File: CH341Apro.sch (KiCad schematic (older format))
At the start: 17 parts, among them J1 USB_A, J3 ZIF-16, J4 , J5 V_SEL, U1 AMS1117-3.3, U2 CH341a, Y1 12M

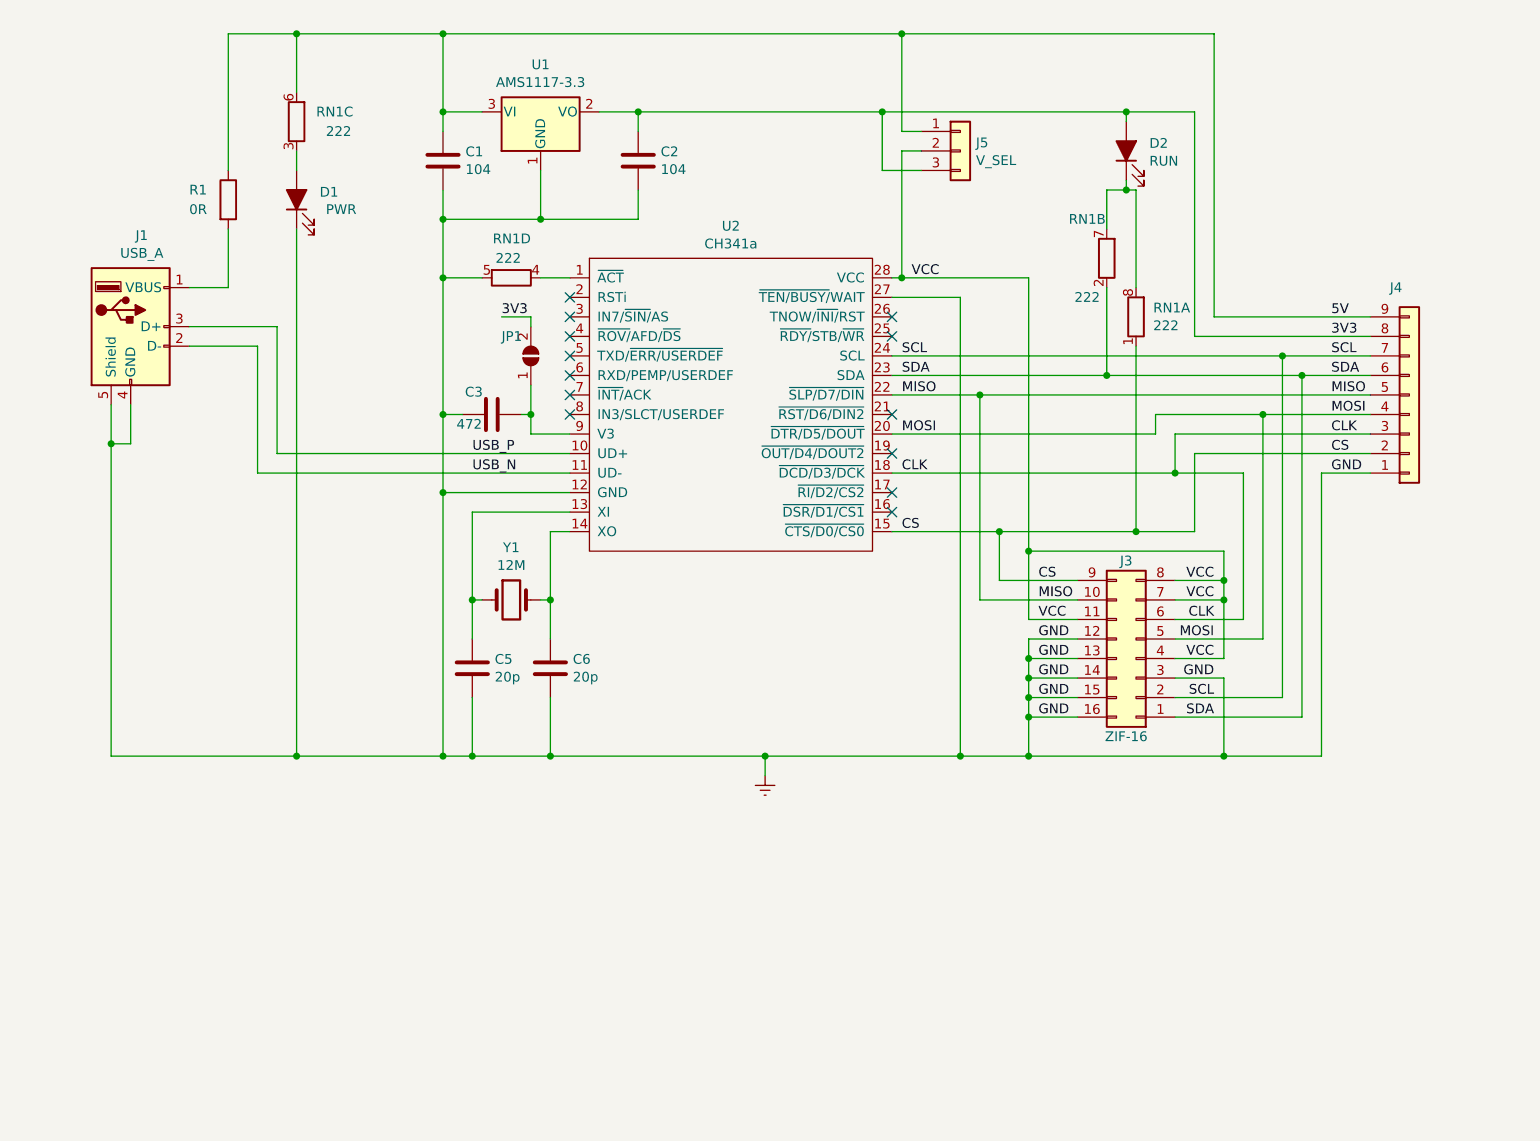
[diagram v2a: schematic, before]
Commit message: Major ergo change
Updated components footprints for hand soldering.
Change VCC routing.
Add JP1/2 for selecting operating voltage.
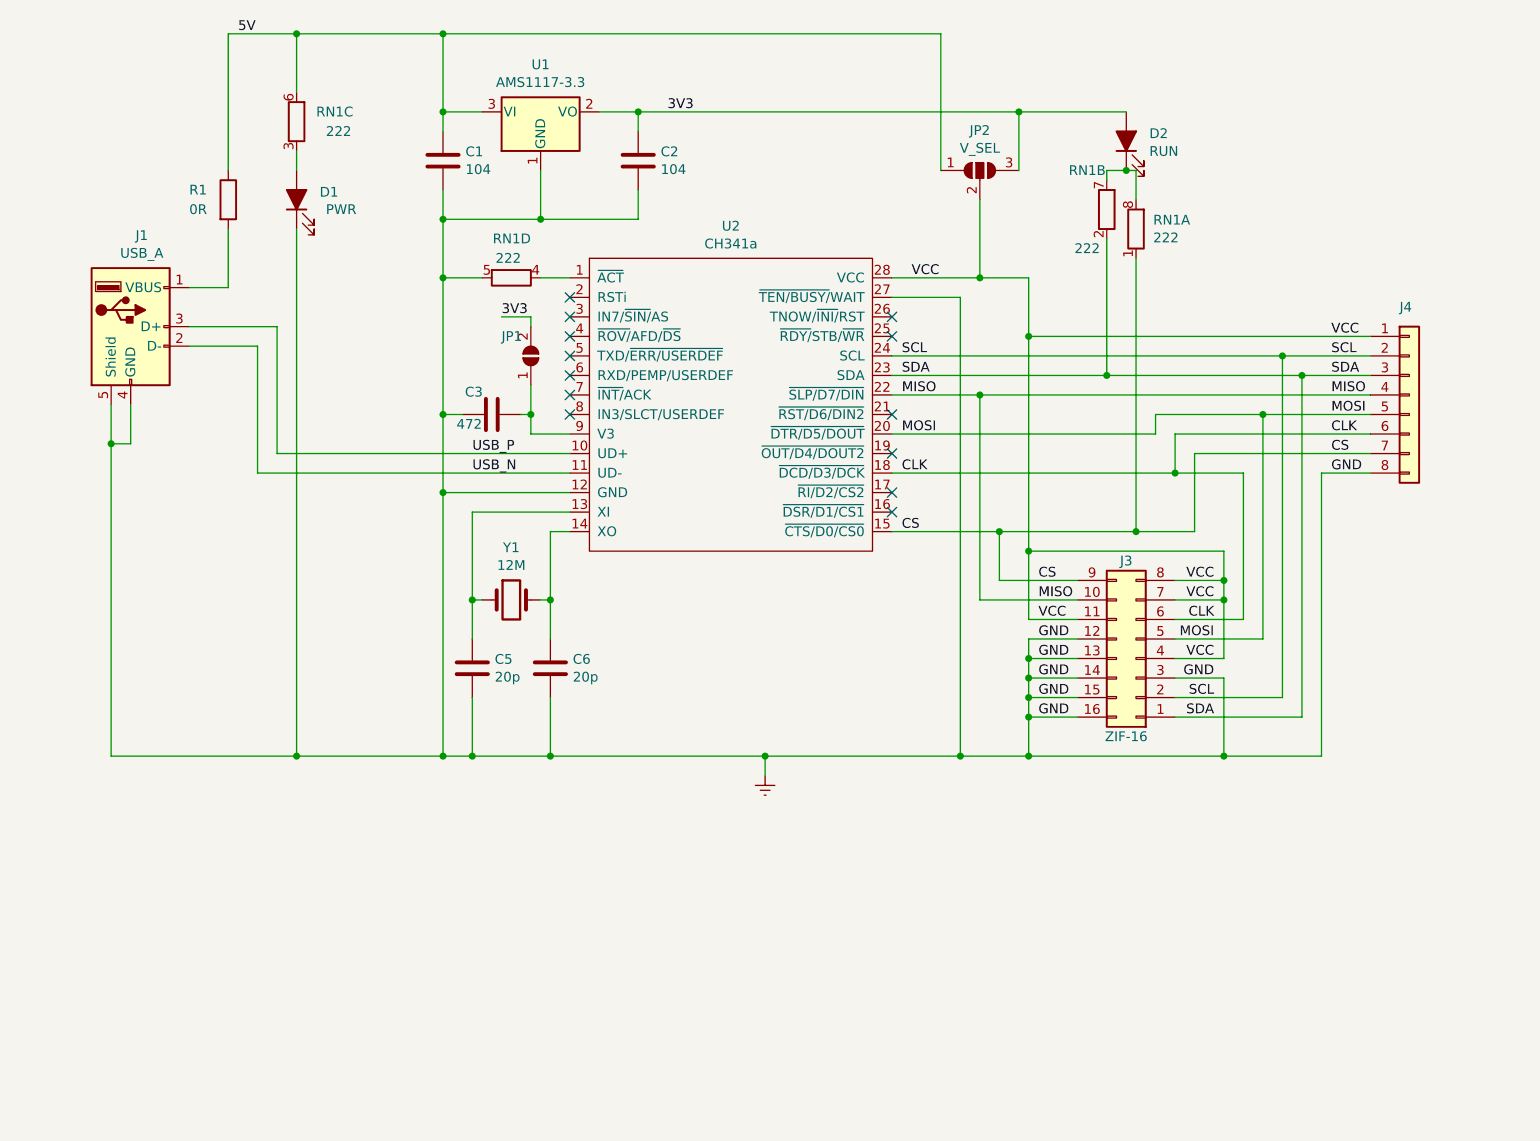
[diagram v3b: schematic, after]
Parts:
- removed J4: (no value), Connector_PinHeader_2.54mm:PinHeader_1x09_P2.54mm_Vertical, symbol Connector_Generic:Conn_01x09
- removed J5: V_SEL, Connector_PinHeader_2.54mm:PinHeader_1x03_P2.54mm_Vertical, symbol Connector_Generic:Conn_01x03
- added J4: (no value), Connector_PinHeader_2.54mm:PinHeader_1x08_P2.54mm_Vertical, symbol Connector_Generic:Conn_01x08
- added JP2: V_SEL, Jumper:SolderJumper-3_P1.3mm_Open_RoundedPad1.0x1.5mm_NumberLabels, symbol Jumper:SolderJumper_3_Open
- C1, C2, C3: footprint Capacitor_SMD:C_0603_1608Metric -> Capacitor_SMD:C_0603_1608Metric_Pad1.05x0.95mm_HandSolder
- C5, C6: footprint Capacitor_SMD:C_0402_1005Metric -> Capacitor_SMD:C_0603_1608Metric_Pad1.05x0.95mm_HandSolder
- D1, D2: footprint LED_SMD:LED_0603_1608Metric -> LED_SMD:LED_0603_1608Metric_Castellated
- JP1: footprint Jumper:SolderJumper-2_P1.3mm_Open_Pad1.0x1.5mm -> Jumper:SolderJumper-2_P1.3mm_Open_RoundedPad1.0x1.5mm
- R1: footprint Resistor_SMD:R_0603_1608Metric -> Resistor_SMD:R_0603_1608Metric_Pad0.98x0.95mm_HandSolder
- Y1: footprint Crystal:Crystal_SMD_5032-2Pin_5.0x3.2mm -> Crystal:Crystal_SMD_5032-2Pin_5.0x3.2mm_HandSoldering
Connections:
- net 3V3: now also JP2.3 (B)
- net 5V: now also JP2.1 (A)
- net CLK: now also J4.6 (Pin_6)
- net CS: now also J4.7 (Pin_7)
- net Earth: now also J4.8 (Pin_8)
- net MISO: now also J4.4 (Pin_4)
- net MOSI: now also J4.5 (Pin_5)
- net SCL: now also J4.2 (Pin_2)
- net SDA: now also J4.3 (Pin_3)
- net VCC: now also J4.1 (Pin_1), JP2.2 (C)
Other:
- moved on the sheet: D2, RN1A, RN1B
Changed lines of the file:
@@
 Sheet 1 1
 Title "CH341A Programmer"
-Date "2021-02-26"
-Rev "V0.2"
+Date "2021-03-12"
+Rev "V0.2a"
 Comp "JackCarterSmith originally from Ray Tracer / Jake L"
 Comment1 ""
@@
 F 0 "R1" H 1150 1550 50  0000 L CNN
 F 1 "0R" H 1150 1450 50  0000 L CNN
-F 2 "Resistor_SMD:R_0603_1608Metric" V 1280 1500 50  0001 C CNN
+F 2 "Resistor_SMD:R_0603_1608Metric_Pad0.98x0.95mm_HandSolder" V 1280 1500 50  0001 C CNN
 F 3 "~" H 1350 1500 50  0001 C CNN
 F 4 "C207010" H 1350 1500 50  0001 C CNN "LCSC"
@@
 L Device:R_Pack04_Split RN1
 U 1 1 5F0C60C3
-P 6000 2100
-F 0 "RN1" H 6088 2146 50  0000 L CNN
-F 1 "222" H 6088 2055 50  0000 L CNN
-F 2 "Resistor_SMD:R_Array_Convex_4x0603" V 5920 2100 50  0001 C CNN
-F 3 "~" H 6000 2100 50  0001 C CNN
-F 4 "C12001" H 6000 2100 50  0001 C CNN "LCSC"
-	1    6000 2100
+P 6000 1650
+F 0 "RN1" H 6088 1696 50  0000 L CNN
+F 1 "222" H 6088 1605 50  0000 L CNN
+F 2 "Resistor_SMD:R_Array_Convex_4x0603" V 5920 1650 50  0001 C CNN
+F 3 "~" H 6000 1650 50  0001 C CNN
+F 4 "C12001" H 6000 1650 50  0001 C CNN "LCSC"
+	1    6000 1650
 	1    0    0    -1
 $EndComp
@@
 L Device:R_Pack04_Split RN1
 U 2 1 5F0C7BA5
-P 5850 1800
-F 0 "RN1" H 5750 2000 50  0000 C CNN
-F 1 "222" H 5750 1600 50  0000 C CNN
-F 2 "Resistor_SMD:R_Array_Convex_4x0603" V 5770 1800 50  0001 C CNN
-F 3 "~" H 5850 1800 50  0001 C CNN
-F 4 "C12001" H 5850 1800 50  0001 C CNN "LCSC"
-	2    5850 1800
+P 5850 1550
+F 0 "RN1" H 5750 1750 50  0000 C CNN
+F 1 "222" H 5750 1350 50  0000 C CNN
+F 2 "Resistor_SMD:R_Array_Convex_4x0603" V 5770 1550 50  0001 C CNN
+F 3 "~" H 5850 1550 50  0001 C CNN
+F 4 "C12001" H 5850 1550 50  0001 C CNN "LCSC"
+	2    5850 1550
 	1    0    0    -1
 $EndComp
@@
 F 0 "C1" H 2565 1346 50  0000 L CNN
 F 1 "104" H 2565 1255 50  0000 L CNN
-F 2 "Capacitor_SMD:C_0603_1608Metric" H 2488 1150 50  0001 C CNN
+F 2 "Capacitor_SMD:C_0603_1608Metric_Pad1.05x0.95mm_HandSolder" H 2488 1150 50  0001 C CNN
 F 3 "~" H 2450 1300 50  0001 C CNN
 F 4 "C19702" H 2450 1300 50  0001 C CNN "LCSC"
@@
 L Device:LED_ALT D2
 U 1 1 5F0CEBAD
-P 5950 1250
-F 0 "D2" V 5989 1132 50  0000 R CNN
-F 1 "RUN" V 5898 1132 50  0000 R CNN
-F 2 "LED_SMD:LED_0603_1608Metric" H 5950 1250 50  0001 C CNN
-F 3 "~" H 5950 1250 50  0001 C CNN
-F 4 "C72043" V 5950 1250 50  0001 C CNN "LCSC"
-	1    5950 1250
+P 5950 1200
+F 0 "D2" V 5989 1082 50  0000 R CNN
+F 1 "RUN" V 5898 1082 50  0000 R CNN
+F 2 "LED_SMD:LED_0603_1608Metric_Castellated" H 5950 1200 50  0001 C CNN
+F 3 "~" H 5950 1200 50  0001 C CNN
+F 4 "C72043" V 5950 1200 50  0001 C CNN "LCSC"
+	1    5950 1200
 	0    -1   -1   0
 $EndComp
-Wire Wire Line
-	5850 1650 5850 1450
-Wire Wire Line
-	5850 1450 5950 1450
-Wire Wire Line
-	5950 1450 5950 1400
-Wire Wire Line
-	5950 1450 6000 1450
-Wire Wire Line
-	6000 1450 6000 1950
-Connection ~ 5950 1450
 $Comp
 L Device:LED_ALT D1
@@
 F 0 "D1" V 1739 1382 50  0000 R CNN
 F 1 "PWR" V 1650 1350 50  0000 R CNN
-F 2 "LED_SMD:LED_0603_1608Metric" H 1700 1500 50  0001 C CNN
+F 2 "LED_SMD:LED_0603_1608Metric_Castellated" H 1700 1500 50  0001 C CNN
 F 3 "~" H 1700 1500 50  0001 C CNN
 F 4 "C72044" V 1700 1500 50  0001 C CNN "LCSC"
@@
 F 0 "C2" H 3565 1346 50  0000 L CNN
 F 1 "104" H 3565 1255 50  0000 L CNN
-F 2 "Capacitor_SMD:C_0603_1608Metric" H 3488 1150 50  0001 C CNN
+F 2 "Capacitor_SMD:C_0603_1608Metric_Pad1.05x0.95mm_HandSolder" H 3488 1150 50  0001 C CNN
 F 3 "~" H 3450 1300 50  0001 C CNN
 F 4 "C19702" H 3450 1300 50  0001 C CNN "LCSC"
@@
 F 0 "Y1" H 2800 3818 50  0000 C CNN
 F 1 "12M" H 2800 3727 50  0000 C CNN
-F 2 "Crystal:Crystal_SMD_5032-2Pin_5.0x3.2mm" H 2800 3550 50  0001 C CNN
+F 2 "Crystal:Crystal_SMD_5032-2Pin_5.0x3.2mm_HandSoldering" H 2800 3550 50  0001 C CNN
 F 3 "~" H 2800 3550 50  0001 C CNN
 F 4 "C112573" H 2800 3550 50  0001 C CNN "LCSC"
@@
 F 0 "C5" H 2715 3946 50  0000 L CNN
 F 1 "20p" H 2715 3855 50  0000 L CNN
-F 2 "Capacitor_SMD:C_0402_1005Metric" H 2638 3750 50  0001 C CNN
+F 2 "Capacitor_SMD:C_0603_1608Metric_Pad1.05x0.95mm_HandSolder" H 2638 3750 50  0001 C CNN
 F 3 "~" H 2600 3900 50  0001 C CNN
 F 4 "C1554" H 2600 3900 50  0001 C CNN "LCSC"
@@
 F 0 "C6" H 3115 3946 50  0000 L CNN
 F 1 "20p" H 3115 3855 50  0000 L CNN
-F 2 "Capacitor_SMD:C_0402_1005Metric" H 3038 3750 50  0001 C CNN
+F 2 "Capacitor_SMD:C_0603_1608Metric_Pad1.05x0.95mm_HandSolder" H 3038 3750 50  0001 C CNN
 F 3 "~" H 3000 3900 50  0001 C CNN
 F 4 "C1554" H 3000 3900 50  0001 C CNN "LCSC"
@@
 	1    0    0    -1
 $EndComp
-Wire Wire Line
-	5850 2400 5850 1950
 $Comp
 L power:Earth #PWR01
@@
 Wire Wire Line
 	2450 1050 2450 650
-Wire Wire Line
-	5950 1100 5950 1050
-Connection ~ 5950 1050
-Wire Wire Line
-	5950 1050 6300 1050
-Text Label 7000 2200 0    50   ~ 0
-3V3
 Text Label 7000 2900 0    50   ~ 0
 GND
@@
 Text Label 7000 2700 0    50   ~ 0
 CLK
-Text Label 7000 2100 0    50   ~ 0
-5V
-Wire Wire Line
-	6400 650  6400 2100
-Wire Wire Line
-	6300 1050 6300 2200
+Text Label 7000 2200 0    50   ~ 0
+VCC
 Text Label 5500 3550 0    50   ~ 0
 MISO
@@
 	750  2550 750  2750
 Connection ~ 750  2750
-Wire Wire Line
-	4750 1900 4800 1900
-Wire Wire Line
-	4800 1900 4800 1250
-Wire Wire Line
-	4800 1250 4900 1250
-Wire Wire Line
-	4900 1350 4700 1350
-Wire Wire Line
-	4700 1350 4700 1050
-Wire Wire Line
-	4900 1150 4800 1150
-Wire Wire Line
-	4800 1150 4800 650
-Connection ~ 4800 650
-Wire Wire Line
-	4800 650  6400 650
 Text Label 2750 2100 0    50   ~ 0
 3V3
@@
 Wire Wire Line
 	2450 1600 2950 1600
-Wire Wire Line
-	2450 650  4800 650
-Wire Wire Line
-	3450 1050 4700 1050
 Connection ~ 3450 1050
-Connection ~ 4700 1050
 Text Label 5500 3850 0    50   ~ 0
 GND
@@
 Wire Wire Line
 	4750 2900 6200 2900
-$Comp
-L Connector_Generic:Conn_01x09 J4
-U 1 1 603FB5BA
-P 7400 2500
-F 0 "J4" H 7300 1950 50  0000 L CNN
-F 1 " " H 7480 2451 50  0000 L CNN
-F 2 "Connector_PinHeader_2.54mm:PinHeader_1x09_P2.54mm_Vertical" H 7400 2500 50  0001 C CNN
-F 3 "~" H 7400 2500 50  0001 C CNN
-	1    7400 2500
-	1    0    0    1
-$EndComp
-Wire Wire Line
-	7200 2100 6400 2100
-$Comp
-L Connector_Generic:Conn_01x03 J5
-U 1 1 604046DB
-P 5100 1250
-F 0 "J5" H 5180 1292 50  0000 L CNN
-F 1 "V_SEL" H 5180 1201 50  0000 L CNN
-F 2 "Connector_PinHeader_2.54mm:PinHeader_1x03_P2.54mm_Vertical" H 5100 1250 50  0001 C CNN
-F 3 "~" H 5100 1250 50  0001 C CNN
-	1    5100 1250
-	1    0    0    -1
-$EndComp
 Wire Wire Line
 	4750 2400 5850 2400
@@
 Wire Wire Line
 	5450 3650 5450 3300
-Wire Wire Line
-	7200 2200 6300 2200
 Wire Wire Line
 	6450 3450 6450 3300
@@
 SDA
 Wire Wire Line
-	6000 2250 6000 3200
-Wire Wire Line
 	7200 2900 6950 2900
 Wire Wire Line
@@
 	6650 2600 6100 2600
 Wire Wire Line
-	4700 1050 5950 1050
-Wire Wire Line
-	4800 1900 5450 1900
-Wire Wire Line
-	5450 1900 5450 3300
-Connection ~ 4800 1900
+	5450 1900 5450 2200
 Connection ~ 5450 3300
 Text Label 4850 1900 0    50   ~ 0
@@
 F 0 "C3" V 2815 2646 50  0000 L CNN
 F 1 "472" V 2650 2650 50  0000 L CNN
-F 2 "Capacitor_SMD:C_0603_1608Metric" H 2738 2450 50  0001 C CNN
+F 2 "Capacitor_SMD:C_0603_1608Metric_Pad1.05x0.95mm_HandSolder" H 2738 2450 50  0001 C CNN
 F 3 "~" H 2700 2600 50  0001 C CNN
 F 4 "C8032" V 2700 2600 50  0001 C CNN "LCSC"
@@
 F 0 "JP1" V 3000 2450 50  0000 R CNN
 F 1 " " V 2855 2212 50  0000 R CNN
-F 2 "Jumper:SolderJumper-2_P1.3mm_Open_Pad1.0x1.5mm" H 2900 2300 50  0001 C CNN
+F 2 "Jumper:SolderJumper-2_P1.3mm_Open_RoundedPad1.0x1.5mm" H 2900 2300 50  0001 C CNN
 F 3 "~" H 2900 2300 50  0001 C CNN
 	1    2900 2300
 	0    -1   -1   0
 $EndComp
+$Comp
+L Jumper:SolderJumper_3_Open JP2
+U 1 1 604BEDAC
+P 5200 1350
+F 0 "JP2" H 5200 1555 50  0000 C CNN
+F 1 "V_SEL" H 5200 1464 50  0000 C CNN
+F 2 "Jumper:SolderJumper-3_P1.3mm_Open_RoundedPad1.0x1.5mm_NumberLabels" H 5200 1350 50  0001 C CNN
+F 3 "~" H 5200 1350 50  0001 C CNN
+	1    5200 1350
+	1    0    0    -1
+$EndComp
+Wire Wire Line
+	2450 650  5000 650
+Wire Wire Line
+	4750 1900 5200 1900
+Wire Wire Line
+	5200 1500 5200 1900
+Connection ~ 5200 1900
+Wire Wire Line
+	5200 1900 5450 1900
+$Comp
+L Connector_Generic:Conn_01x08 J4
+U 1 1 604F57DB
+P 7400 2500
+F 0 "J4" H 7350 2950 50  0000 L CNN
+F 1 " " H 7480 2401 50  0000 L CNN
+F 2 "Connector_PinHeader_2.54mm:PinHeader_1x08_P2.54mm_Vertical" H 7400 2500 50  0001 C CNN
+F 3 "~" H 7400 2500 50  0001 C CNN
+	1    7400 2500
+	1    0    0    -1
+$EndComp
+Wire Wire Line
+	3450 1050 5400 1050
+Wire Wire Line
+	5000 1350 5000 650
+Wire Wire Line
+	5400 1350 5400 1050
+Connection ~ 5400 1050
+Wire Wire Line
+	5400 1050 5950 1050
+Wire Wire Line
+	5950 1350 5850 1350
+Wire Wire Line
+	5850 1350 5850 1400
+Wire Wire Line
+	5950 1350 6000 1350
+Wire Wire Line
+	6000 1350 6000 1500
+Connection ~ 5950 1350
+Wire Wire Line
+	5850 1700 5850 2400
+Wire Wire Line
+	6000 1800 6000 3200
+Wire Wire Line
+	5450 2200 7200 2200
+Connection ~ 5450 2200
+Wire Wire Line
+	5450 2200 5450 3300
+Text Label 3600 1050 0    50   ~ 0
+3V3
+Text Label 1400 650  0    50   ~ 0
+5V
 $EndSCHEMATC

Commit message: Changed drawing and placement
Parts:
- J1: symbol CH341Apro-rescue:USB_A-Connector-CH341Apro-rescue -> CH341Apro-rescue:USB_A-Connector-CH341Apro-rescue-CH341Apro-rescue
- JP1: footprint Jumper:SolderJumper-2_P1.3mm_Open_RoundedPad1.0x1.5mm -> Connector_PinHeader_2.54mm:PinHeader_1x02_P2.54mm_Vertical
- JP2: footprint Jumper:SolderJumper-3_P1.3mm_Open_RoundedPad1.0x1.5mm_NumberLabels -> Connector_PinHeader_2.54mm:PinHeader_1x03_P2.54mm_Vertical
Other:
- moved on the sheet: RN1A, RN1B
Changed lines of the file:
@@
 L Device:R_Pack04_Split RN1
 U 1 1 5F0C60C3
-P 6000 1650
-F 0 "RN1" H 6088 1696 50  0000 L CNN
-F 1 "222" H 6088 1605 50  0000 L CNN
-F 2 "Resistor_SMD:R_Array_Convex_4x0603" V 5920 1650 50  0001 C CNN
-F 3 "~" H 6000 1650 50  0001 C CNN
-F 4 "C12001" H 6000 1650 50  0001 C CNN "LCSC"
-	1    6000 1650
+P 6000 1950
+F 0 "RN1" H 6088 1996 50  0000 L CNN
+F 1 "222" H 6088 1905 50  0000 L CNN
+F 2 "Resistor_SMD:R_Array_Convex_4x0603" V 5920 1950 50  0001 C CNN
+F 3 "~" H 6000 1950 50  0001 C CNN
+F 4 "C12001" H 6000 1950 50  0001 C CNN "LCSC"
+	1    6000 1950
 	1    0    0    -1
 $EndComp
@@
 L Device:R_Pack04_Split RN1
 U 2 1 5F0C7BA5
-P 5850 1550
-F 0 "RN1" H 5750 1750 50  0000 C CNN
-F 1 "222" H 5750 1350 50  0000 C CNN
-F 2 "Resistor_SMD:R_Array_Convex_4x0603" V 5770 1550 50  0001 C CNN
-F 3 "~" H 5850 1550 50  0001 C CNN
-F 4 "C12001" H 5850 1550 50  0001 C CNN "LCSC"
-	2    5850 1550
+P 5850 1650
+F 0 "RN1" H 5700 1700 50  0000 C CNN
+F 1 "222" H 5700 1600 50  0000 C CNN
+F 2 "Resistor_SMD:R_Array_Convex_4x0603" V 5770 1650 50  0001 C CNN
+F 3 "~" H 5850 1650 50  0001 C CNN
+F 4 "C12001" H 5850 1650 50  0001 C CNN "LCSC"
+	2    5850 1650
 	1    0    0    -1
 $EndComp
@@
 GND
 $Comp
-L CH341Apro-rescue:USB_A-Connector-CH341Apro-rescue J1
+L CH341Apro-rescue:USB_A-Connector-CH341Apro-rescue-CH341Apro-rescue J1
 U 1 1 5F58AEC8
 P 850 2150
@@
 	4750 2900 6200 2900
 Wire Wire Line
-	4750 2400 5850 2400
-Wire Wire Line
-	5850 2400 6850 2400
-Connection ~ 5850 2400
-Wire Wire Line
 	4750 2300 6750 2300
 Wire Wire Line
@@
 	5300 3450 5300 3200
 Connection ~ 5300 3200
-Wire Wire Line
-	5300 3200 6000 3200
 Wire Wire Line
 	5700 3650 5450 3650
@@
 Wire Wire Line
 	6300 2800 6300 3200
-Wire Wire Line
-	6300 3200 6000 3200
-Connection ~ 6000 3200
 Wire Wire Line
 	6650 3750 6650 2600
@@
 F 0 "JP1" V 3000 2450 50  0000 R CNN
 F 1 " " V 2855 2212 50  0000 R CNN
-F 2 "Jumper:SolderJumper-2_P1.3mm_Open_RoundedPad1.0x1.5mm" H 2900 2300 50  0001 C CNN
+F 2 "Connector_PinHeader_2.54mm:PinHeader_1x02_P2.54mm_Vertical" H 2900 2300 50  0001 C CNN
 F 3 "~" H 2900 2300 50  0001 C CNN
 	1    2900 2300
@@
 F 0 "JP2" H 5200 1555 50  0000 C CNN
 F 1 "V_SEL" H 5200 1464 50  0000 C CNN
-F 2 "Jumper:SolderJumper-3_P1.3mm_Open_RoundedPad1.0x1.5mm_NumberLabels" H 5200 1350 50  0001 C CNN
+F 2 "Connector_PinHeader_2.54mm:PinHeader_1x03_P2.54mm_Vertical" H 5200 1350 50  0001 C CNN
 F 3 "~" H 5200 1350 50  0001 C CNN
 	1    5200 1350
@@
 	5400 1050 5950 1050
 Wire Wire Line
-	5950 1350 5850 1350
-Wire Wire Line
-	5850 1350 5850 1400
-Wire Wire Line
-	5950 1350 6000 1350
-Wire Wire Line
-	6000 1350 6000 1500
-Connection ~ 5950 1350
-Wire Wire Line
-	5850 1700 5850 2400
-Wire Wire Line
-	6000 1800 6000 3200
-Wire Wire Line
 	5450 2200 7200 2200
 Connection ~ 5450 2200
@@
 Text Label 1400 650  0    50   ~ 0
 5V
+Wire Wire Line
+	5300 3200 6000 3200
+Wire Wire Line
+	6000 2100 6000 3200
+Connection ~ 6000 3200
+Wire Wire Line
+	6000 3200 6300 3200
+Wire Wire Line
+	4750 2400 5850 2400
+Wire Wire Line
+	5850 1800 5850 2400
+Connection ~ 5850 2400
+Wire Wire Line
+	5850 2400 6850 2400
+Wire Wire Line
+	5850 1500 5850 1450
+Wire Wire Line
+	5850 1450 5950 1450
+Wire Wire Line
+	5950 1450 5950 1350
+Wire Wire Line
+	5950 1450 6000 1450
+Wire Wire Line
+	6000 1450 6000 1800
+Connection ~ 5950 1450
 $EndSCHEMATC
